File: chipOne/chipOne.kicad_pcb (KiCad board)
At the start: 2 copper layers, 116.8 x 106.7 mm, 25 parts, among them J1 BNC, J2 BNC, U1 Y1247AstimulusGenerator, U10A1 3pinSwitchCustom, U2 Y1247AstimulusGenerator, U3 Y1247AstimulusGenerator, U4 Y1247AstimulusGenerator, U5 CHIP1, U6 3pinSwitchCustom

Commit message: Layout for PCB one made : stage 1
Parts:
- added J3: 5767007-8, U4164AlogicAnalyser:TE_5767007-8, F.Cu at (39.4, 141.0)
- added J4: 5767007-8, U4164AlogicAnalyser:TE_5767007-8, F.Cu at (118.1, 141.0)
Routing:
- net I_clk: track 50.5 -> 196.1 mm
- net I_inData3: track 52.3 -> 152.0 mm, vias 1 -> 2
- net I_address2: track 29.9 -> 120.3 mm, vias 1 -> 3
- net I_address3: track 39.8 -> 127.7 mm, vias 2 -> 4
- net I_address0: track 31.2 -> 118.3 mm, vias 0 -> 2
- net I_address5: track 46.5 -> 130.1 mm, vias 2 -> 3
- net I_address4: track 27.8 -> 109.4 mm, vias 2 -> 4
- net VSSQ: track 599.2 -> 676.0 mm
- net I_address1: track 31.1 -> 107.1 mm
- net B_inData_bi5: track 24.5 -> 95.1 mm, vias 0 -> 2
- net I_SEL1: track 23.4 -> 91.8 mm, vias 0 -> 1
- net VDDQ: track 41.9 -> 102.4 mm, vias 0 -> 1
- net B_inData_bi2: track 33.9 -> 91.5 mm, vias 0 -> 2
- net I_enable: track 26.0 -> 81.3 mm, vias 0 -> 1
- net I_SEL2: track 37.8 -> 92.7 mm, vias 2 -> 3
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
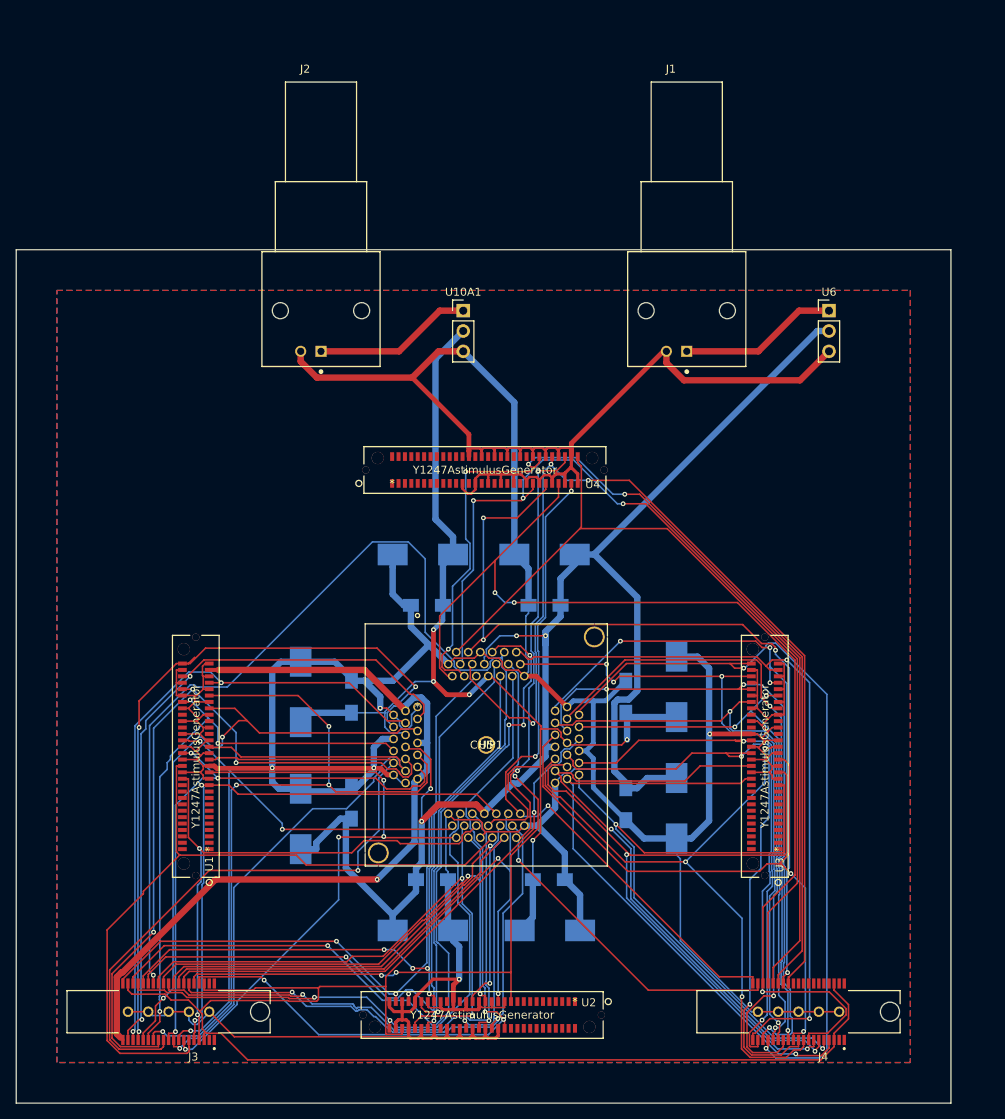
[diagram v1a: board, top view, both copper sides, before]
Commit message: Layout Done and routings made
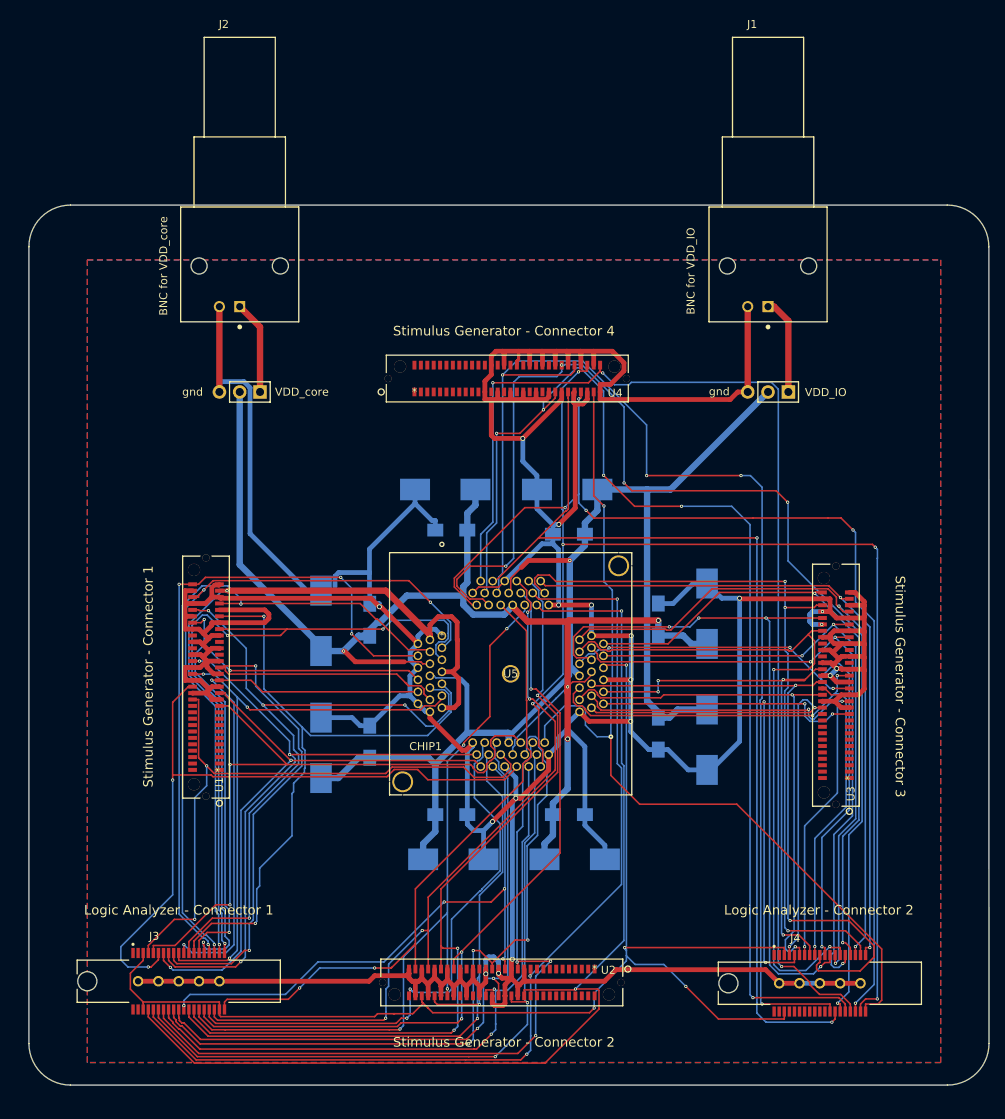
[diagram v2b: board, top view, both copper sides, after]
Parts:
- moved U10A1 27.4 mm to (50.8, 63.5), turned to 270 degrees
- moved U3 12.6 mm to (124.5, 111.8)
- moved U4 11.8 mm to (70.1, 63.5)
- moved J2 11.6 mm to (48.3, 52.8)
- moved J1 11.6 mm to (114.3, 52.8)
- moved U6 11.4 mm to (116.8, 63.5), turned to 270 degrees
- moved C14 10.5 mm to (100.6, 91.9)
- moved U1 9.99 mm to (45.7, 110.7)
- moved C16 9.91 mm to (106.7, 91.2)
- moved C13 9.89 mm to (64.5, 92.0)
- moved C6 9.88 mm to (74.7, 80.8)
- moved C10 9.72 mm to (100.6, 106.2)
- moved C3 9.67 mm to (75.0, 121.9)
- moved C7 9.42 mm to (90.1, 121.9)
- moved C2 9.40 mm to (89.4, 81.3)
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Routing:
- net B_outData_bi7: track 94.8 -> 153.5 mm, vias 3 -> 5
- net VSSQ: track 676.0 -> 733.2 mm, vias 5 -> 18
- net I_inData3: track 152.0 -> 103.7 mm, vias 2 -> 3
- net B_inData_bi1: track 92.1 -> 135.8 mm, vias 3 -> 2
- net I_address1: track 107.1 -> 147.6 mm, vias 0 -> 3
- net B_inData_bi0: track 86.5 -> 124.0 mm
- net I_clk: track 196.1 -> 162.4 mm, vias 1 -> 4
- net VDD_IO: track 194.1 -> 161.7 mm, vias 4 -> 1
- net B_outData_bi6: track 86.0 -> 115.6 mm, vias 3 -> 2
- net I_address3: track 127.7 -> 153.5 mm, vias 4 -> 5
- net I_address2: track 120.3 -> 145.5 mm, vias 3 -> 5
- net I_address5: track 130.1 -> 155.1 mm, vias 3 -> 4
- net I_SEL1: track 91.8 -> 68.8 mm, vias 1 -> 2
- net O_outData6: track 72.9 -> 93.9 mm, vias 2 -> 3
- net I_FCLK: track 76.9 -> 96.1 mm, vias 2 -> 3
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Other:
- board size 116.8 x 106.7 mm -> 120 x 110 mm
- net class Default: via_dia 0.6 -> 0.4; via_drill 0.4 -> 0.2
- net class Power: trace_width 0.8 -> 0.6
- rule via_min_drill: 0.3 -> 0.2
- rule via_min_size: 0.4 -> 0.2
- board text added: "BNC for VDD_IO"
- board text added: "BNC for VDD_core"
- board text added: "Logic Analyzer - Connector 1"
- board text added: "Logic Analyzer - Connector 2"
- board text added: "Stimulus Generator - Connector 1"
- board text added: "Stimulus Generator - Connector 2"
- board text added: "Stimulus Generator - Connector 3"
- board text added: "Stimulus Generator - Connector 4"
- board text added: "VDD_IO"
- board text added: "VDD_core"
- board text added: "gnd"

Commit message: PCB Layout Done and Dusted !
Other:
- board text added: "1"
- board text added: "38"
- board text added: "60"
- board text added: "PCB Designed for Chip 1"

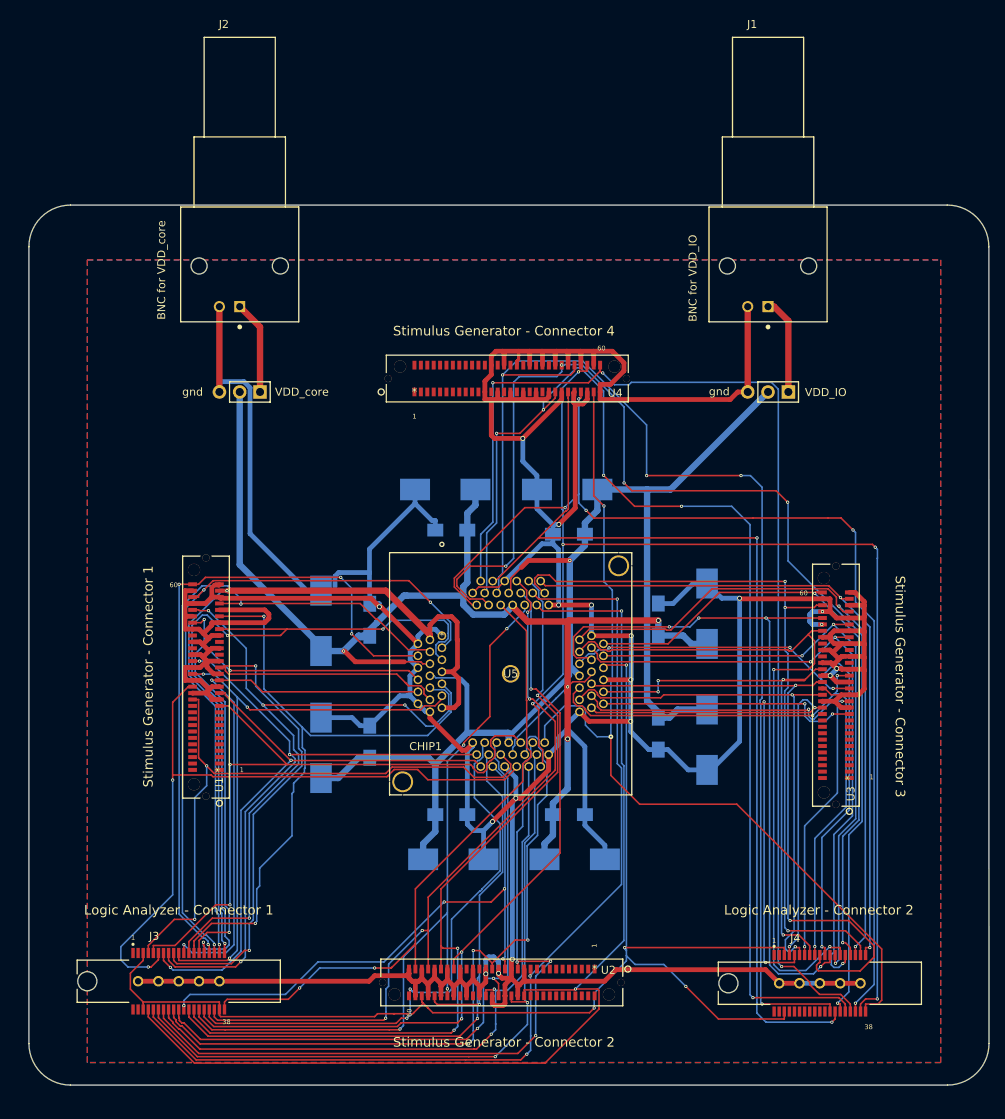
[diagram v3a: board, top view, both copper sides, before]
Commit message: Chip Two design and schematic completed
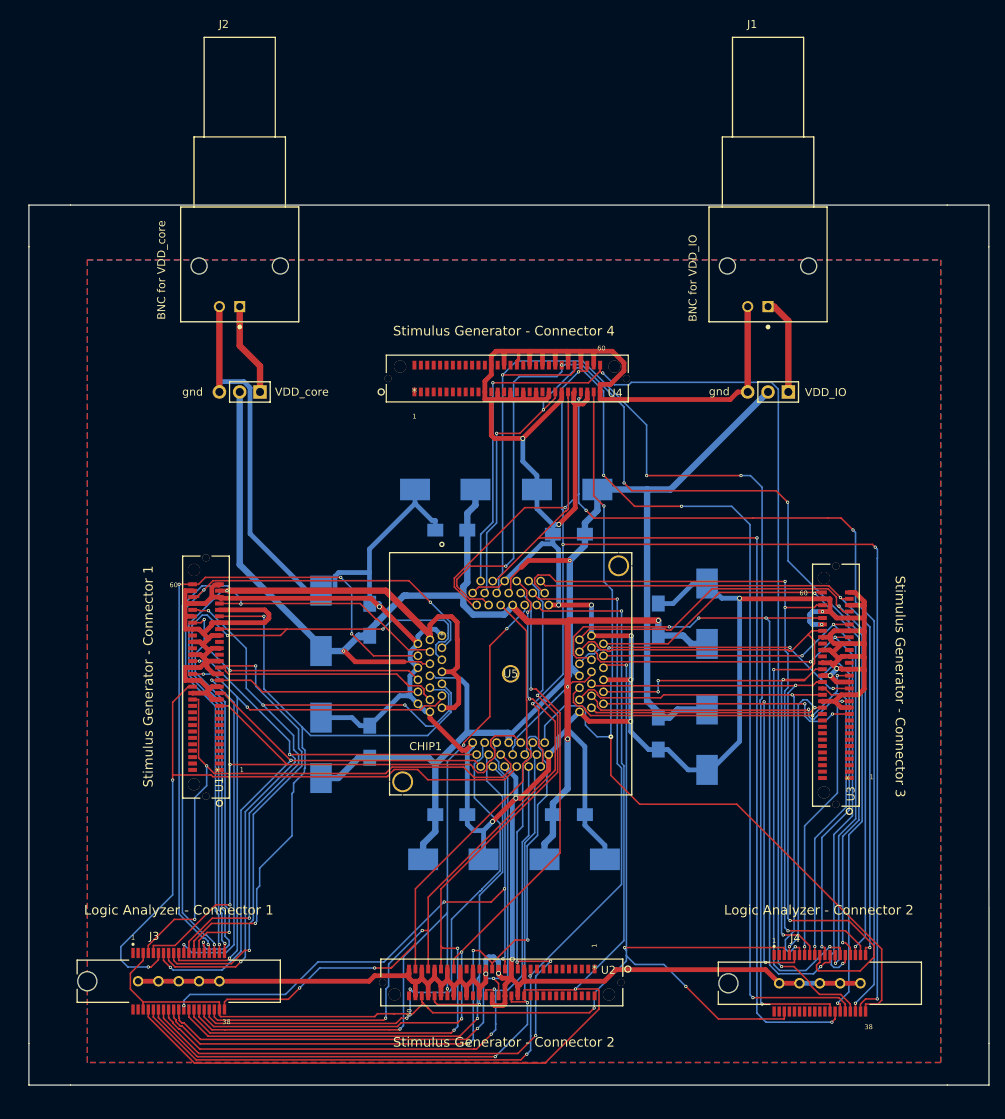
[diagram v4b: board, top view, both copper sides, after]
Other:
- outline, holes or cut-outs redrawn
